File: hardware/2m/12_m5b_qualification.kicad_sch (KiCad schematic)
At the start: 12 parts, among them U950 TLV76701DRVR

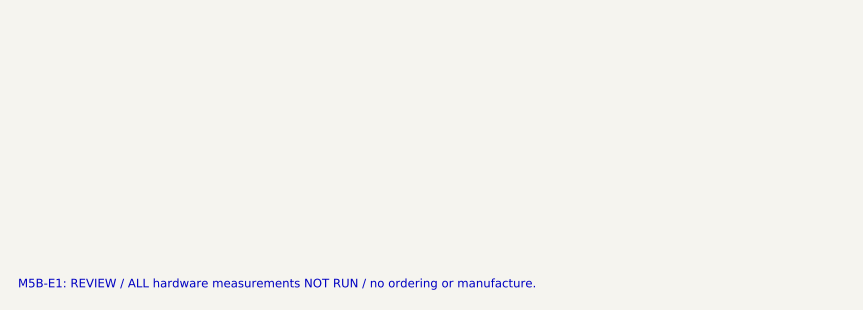
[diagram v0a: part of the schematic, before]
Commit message: Implement M5B-E3 standard JLCPCB RF2M evaluation board
Recalculate and implement 1.6 mm / 1 oz RF geometry, power copper, thermal vias, connector holes and manufacturing legend. Preserve electrical functions and population variants. Add native-geometry DFM, regression checks and fresh native/fabrication review archives. CAD milestone only; no manufacturing or operational release.
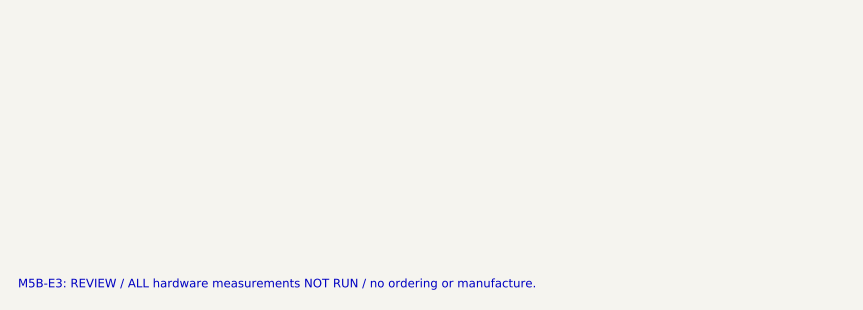
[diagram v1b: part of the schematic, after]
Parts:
- C950, C951: footprint Capacitor_SMD:C_0805_2012Metric -> ARDF_2M:C_0805_2012Metric_E3
- C960, C961: footprint Capacitor_SMD:C_1210_3225Metric -> ARDF_2M:C_1210_3225Metric_E3
- R650, R950, R951: footprint Resistor_SMD:R_0603_1608Metric -> ARDF_2M:R_0603_1608Metric_E3
- R651, R952: footprint Resistor_SMD:R_1206_3216Metric -> ARDF_2M:R_1206_3216Metric_E3
- TP950, TP951: footprint TestPoint:TestPoint_Pad_D1.0mm -> ARDF_2M:TestPoint_Pad_D1.0mm_E3
- U950: footprint Package_SON:WSON-6-1EP_2x2mm_P0.65mm_EP1x1.6mm -> ARDF_2M:WSON-6-1EP_2x2mm_P0.65mm_EP1x1.6mm_E3
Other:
- note added: "M5B-E3: REVIEW / ALL hardware measurements NOT RUN / no ordering or manufacture."
- note removed: "M5B-E1: REVIEW / ALL hardware measurements NOT RUN / no ordering or manufacture."

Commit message: Implement M5B-E4 thermal candidate with source-joint assembly hold
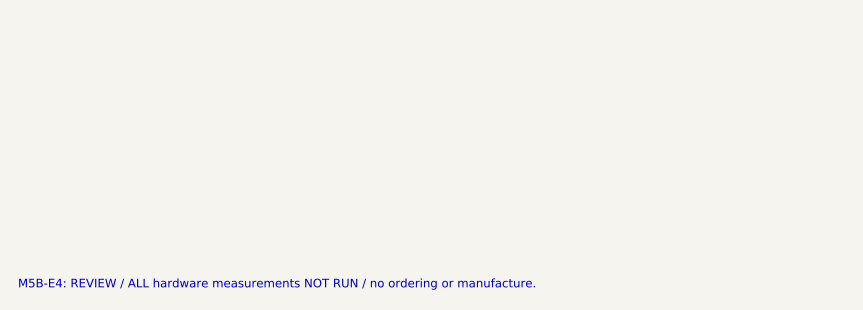
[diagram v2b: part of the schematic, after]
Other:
- note added: "M5B-E4: REVIEW / ALL hardware measurements NOT RUN / no ordering or manufacture."
- note removed: "M5B-E3: REVIEW / ALL hardware measurements NOT RUN / no ordering or manufacture."

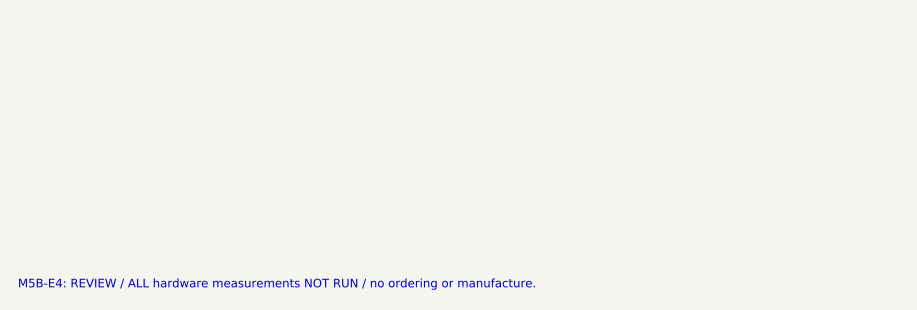
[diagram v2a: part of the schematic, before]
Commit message: Implement M5B-E4R1 source-joint prototype candidate
Replace source mask islands with a controlled open-via hybrid and native-derived local stencil. Preserve standard JLCPCB and RF circuitry. Add assembly qualification, thermal convergence and adverse sensitivities, native DFM/mutation checks and fresh review exports. Conservative 110 C target is missed; 125 C physical gate stays open. No acceptance tag or manufacturing authorization.
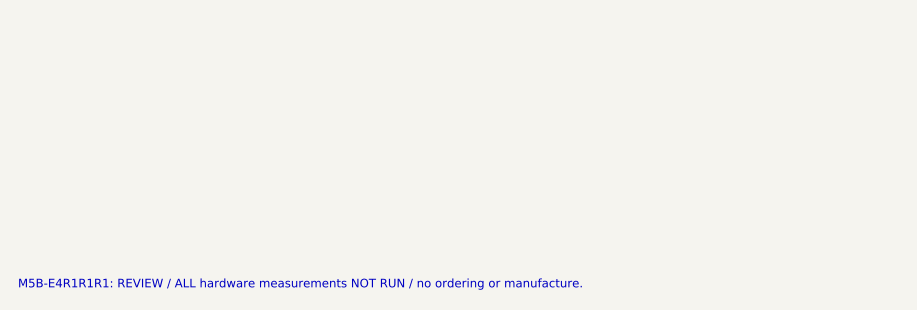
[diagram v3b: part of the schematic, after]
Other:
- note added: "M5B-E4R1R1R1: REVIEW / ALL hardware measurements NOT RUN / no ordering or manufacture."
- note removed: "M5B-E4: REVIEW / ALL hardware measurements NOT RUN / no ordering or manufacture."

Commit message: M5B-E5: compact RF2M to the shared 150x110 mm platform
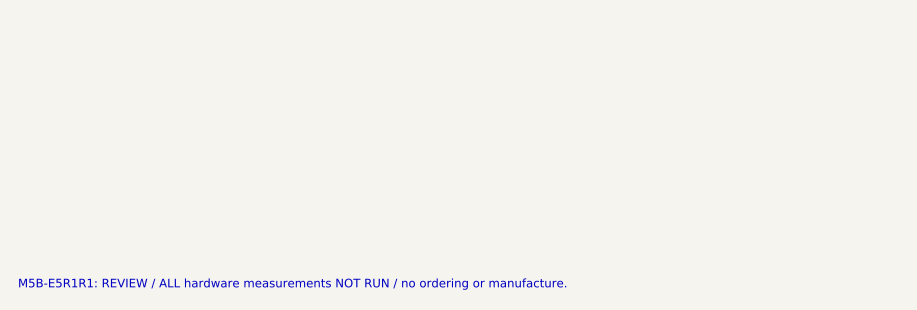
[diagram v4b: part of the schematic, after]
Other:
- note added: "M5B-E5R1R1: REVIEW / ALL hardware measurements NOT RUN / no ordering or manufacture."
- note removed: "M5B-E4R1R1R1: REVIEW / ALL hardware measurements NOT RUN / no ordering or manufacture."

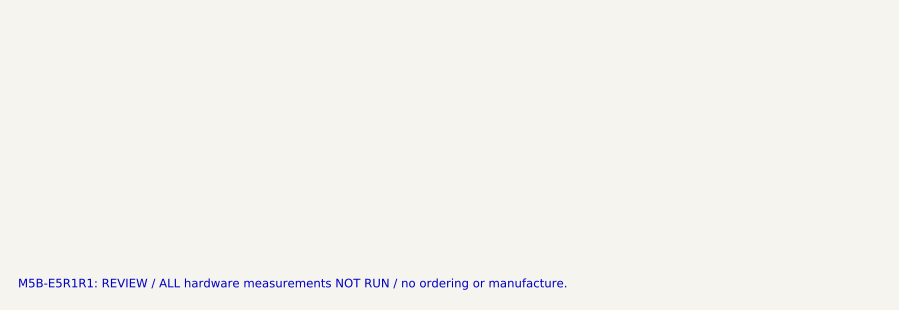
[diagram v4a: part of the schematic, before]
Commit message: M5B-E6R2: Implement carrier-keyed RF2M and unified cooling
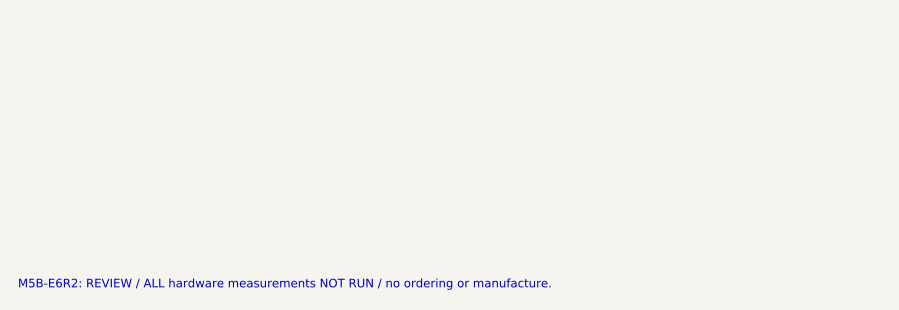
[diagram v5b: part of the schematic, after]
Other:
- note added: "M5B-E6R2: REVIEW / ALL hardware measurements NOT RUN / no ordering or manufacture."
- note removed: "M5B-E5R1R1: REVIEW / ALL hardware measurements NOT RUN / no ordering or manufacture."
